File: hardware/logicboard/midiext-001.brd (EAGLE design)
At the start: 72 x 72 mm, 19 parts, among them IC1 74LS07N, IC2 LTC485N, IC3 LTC485N, X1 JST-2PINPH

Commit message: New schematic.
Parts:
- removed C6: 103, rcl:C025-025X050
- removed J5, J6: (no value), SparkFun-Connectors:2X4
- removed X1: JST-2PINPH, con-jst:B2B-PH
- added CN1, CN3, CN4: (no value), adafruit:JST-PH-2-SMT-RA
- added CN2, CN5: (no value), adafruit:JSTPH3
- moved IC2 33.9 mm to (41.9, 19.1)
- moved IC3 33.9 mm to (34.3, 52.1)
- renumbered D2 to D1, R10 to R2, R6 to R3, R7 to R1, R8 to R5, R9 to R4
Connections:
- removed net COM3: IC2.4
- removed net COM4: IC3.1
- removed net COM5: J6.8
- removed net VDD: X1.P1
- net COM1: now also IC2.1
- net COM2: now also IC3.4
- net GND: now also CN1.2, CN2.2, CN5.2, IC2.2, IC2.3, IC2.4; no longer C6.2, IC3.2, IC3.3, IC3.4, J5.2, J6.2, X1.P2
- net MIDIRX+: now also CN3.1; no longer J6.4
- net MIDIRX-: now also CN3.2; no longer J6.5
- net MIDITX+: now also CN2.1, R2.1; no longer J5.4, R2.2
- net MIDITX-: now also CN2.3; no longer J5.5
- net RX+: now also CN4.1, IC2.6; no longer IC3.6, J6.6
- net RX-: now also CN4.2, IC2.7; no longer IC3.7, J6.7
- net TX+: now also CN5.1, IC3.6; no longer IC2.6, J5.6
- net TX-: now also CN5.3, IC3.7; no longer IC2.7, J5.7
- net VCC: now also CN1.1, IC3.2, IC3.3, R2.2; no longer C6.1, IC2.2, IC2.3, R2.1

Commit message: Changed connectors.
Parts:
- removed CN1, CN3, CN4: (no value), adafruit:JST-PH-2-SMT-RA
- removed CN2, CN5: (no value), adafruit:JSTPH3
- added J1, J2, J3: (no value), SparkFun-Connectors:JST-2-PTH
- added J4, J5: (no value), SparkFun-Connectors:JST-3-PTH
- added J6: (no value), SparkFun-Connectors:JST-4-PTH
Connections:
- net GND: now also J1.2, J4.2, J5.2; no longer CN1.2, CN2.2, CN5.2
- net MIDIRX+: now also J2.1; no longer CN3.1
- net MIDIRX-: now also J2.2; no longer CN3.2
- net MIDITX+: now also J4.1; no longer CN2.1
- net MIDITX-: now also J4.3; no longer CN2.3
- net RX+: now also J3.1; no longer CN4.1
- net RX-: now also J3.2; no longer CN4.2
- net TX+: now also J5.1; no longer CN5.1
- net TX-: now also J5.3; no longer CN5.3
- net VCC: now also J1.1; no longer CN1.1

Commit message: Now has LED indicator port.
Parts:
- added R6, R7, R9: 220, resistor:0204/5
- added R8: 120, resistor:0204/5
- IC1: value 74LS07N -> 74ALS05N; device 74xx-us:DIL14 -> 74xx-eu:DIL14
- J2: device SparkFun-Connectors:JST-2-PTH -> SparkFun-Connectors:JST-3-PTH
- J4: device SparkFun-Connectors:JST-3-PTH -> SparkFun-Connectors:JST-2-PTH
- J5: device SparkFun-Connectors:JST-3-PTH -> SparkFun-Connectors:JST-4-PTH
- J6: device SparkFun-Connectors:JST-4-PTH -> SparkFun-Connectors:JST-3-PTH
- R4: value 120 -> 220
- moved IC1 175.6 mm to (15.2, -119.4)
- moved R4 154.6 mm to (10.2, -137.2)
- moved R5 48.9 mm to (48.3, 12.7)
- moved J2 35.6 mm to (10.2, -63.5)
- moved J5 18.0 mm to (12.7, -99.1)
- moved J6 18.0 mm to (10.2, -81.3)
- moved J4 17.8 mm to (10.2, -45.7)
- moved J3 17.8 mm to (10.2, -27.9)
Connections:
- removed net COM1: IC1.1, IC2.1
- new net N$1: IC1.3, IC1.9, IC2.1
- new net N$10: J5.2, R9.2
- new net N$3: IC1.1, IC1.4, R4.1
- new net N$6: IC1.6, R7.1
- new net N$7: IC1.8, R6.1
- new net N$8: J5.4, R7.2
- new net N$9: J5.3, R6.2
- net COM2: now also IC1.5
- net GND: now also J2.2, J6.2, R9.1; no longer IC1.3, IC1.5, IC1.9, J4.2, J5.2
- net MIDIRX+: now also J3.1; no longer J2.1
- net MIDIRX-: now also J3.2; no longer J2.2
- net MIDITX+: now also J2.1; no longer J4.1
- net MIDITX-: now also J2.3; no longer J4.3
- net RX+: now also J4.1, R5.2; no longer J3.1, R4.2
- net RX-: now also J4.2, R5.1; no longer J3.2, R4.1
- net TX+: now also J6.1, R8.2; no longer J5.1, R5.2
- net TX-: now also J6.3, R8.1; no longer J5.3, R5.1
- net VCC: now also J5.1, R4.2

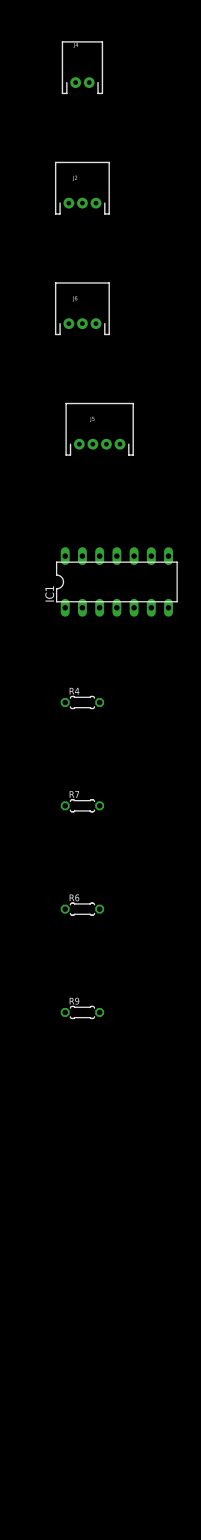
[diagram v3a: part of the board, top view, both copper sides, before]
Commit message: Now has LED indicator panel.
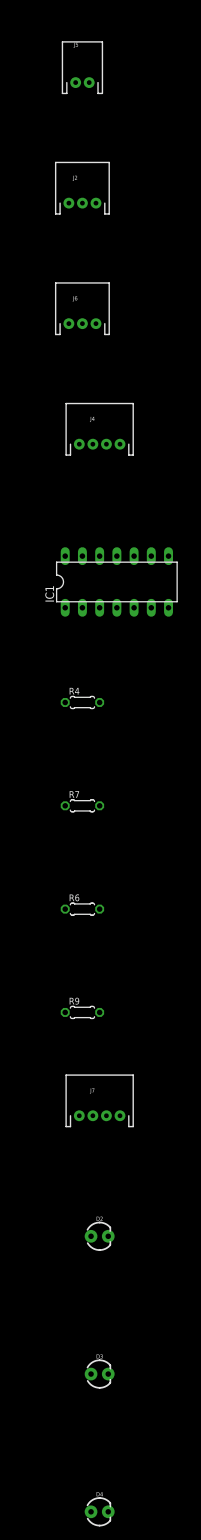
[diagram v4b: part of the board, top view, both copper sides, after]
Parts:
- added D2, D3, D4: (no value), SparkFun-LED:LED_3MM
- added J7: LED, SparkFun-Connectors:JST-4-PTH
- J1: value (none) -> PWR
- J2: value (none) -> MIDIOUT
- J3: value (none) -> MIDIIN
- J4: value (none) -> LED; device SparkFun-Connectors:JST-2-PTH -> SparkFun-Connectors:JST-4-PTH
- J5: value (none) -> MIDIRX; device SparkFun-Connectors:JST-4-PTH -> SparkFun-Connectors:JST-2-PTH
- J6: value (none) -> MIDITX
- moved J4 53.4 mm to (12.7, -99.1)
- moved J5 53.4 mm to (10.2, -45.7)
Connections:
- new net N$11: D3.K, J7.3
- new net N$12: D4.K, J7.4
- new net N$4: D2.A, D3.A, D4.A, J7.1
- new net N$5: D2.K, J7.2
- net N$10: now also J4.2; no longer J5.2
- net N$8: now also J4.4; no longer J5.4
- net N$9: now also J4.3; no longer J5.3
- net RX+: now also J5.1; no longer J4.1
- net RX-: now also J5.2; no longer J4.2
- net VCC: now also J4.1; no longer J5.1
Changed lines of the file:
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@@
 <element name="R1" library="resistor" library_urn="urn:adsk.eagle:library:348" package="0204/5" package3d_urn="urn:adsk.eagle:package:25955/1" value="220" x="40.64" y="63.5"/>
 <element name="R8" library="resistor" library_urn="urn:adsk.eagle:library:348" package="0204/5" package3d_urn="urn:adsk.eagle:package:25955/1" value="120" x="40.64" y="60.96"/>
-<element name="J1" library="SparkFun-Connectors" package="JST-2-PTH" value="" x="10.16" y="-10.16">
+<element name="J1" library="SparkFun-Connectors" package="JST-2-PTH" value="PWR" x="10.16" y="-10.16">
 <attribute name="PROD_ID" value="CONN-09863" x="10.16" y="-10.16" size="1.778" layer="27" display="off"/>
 <attribute name="SKU" value="PRT-09914" x="10.16" y="-10.16" size="1.778" layer="27" display="off"/>
 </element>
-<element name="J3" library="SparkFun-Connectors" package="JST-2-PTH" value="" x="10.16" y="-27.94">
+<element name="J3" library="SparkFun-Connectors" package="JST-2-PTH" value="MIDIIN" x="10.16" y="-27.94">
 <attribute name="PROD_ID" value="CONN-09863" x="10.16" y="-27.94" size="1.778" layer="27" display="off"/>
 <attribute name="SKU" value="PRT-09914" x="10.16" y="-27.94" size="1.778" layer="27" display="off"/>
 </element>
-<element name="J4" library="SparkFun-Connectors" package="JST-2-PTH" value="" x="10.16" y="-45.72">
+<element name="J5" library="SparkFun-Connectors" package="JST-2-PTH" value="MIDIRX" x="10.16" y="-45.72">
 <attribute name="PROD_ID" value="CONN-09863" x="10.16" y="-45.72" size="1.778" layer="27" display="off"/>
 <attribute name="SKU" value="PRT-09914" x="10.16" y="-45.72" size="1.778" layer="27" display="off"/>
 </element>
-<element name="J2" library="SparkFun-Connectors" package="JST-3-PTH" value="" x="10.16" y="-63.5">
+<element name="J2" library="SparkFun-Connectors" package="JST-3-PTH" value="MIDIOUT" x="10.16" y="-63.5">
 <attribute name="PROD_ID" value="WIRE-10037" x="10.16" y="-63.5" size="1.778" layer="27" display="off"/>
 <attribute name="SF_ID" value="PRT-09915" x="10.16" y="-63.5" size="1.778" layer="27" display="off"/>
 </element>
-<element name="J6" library="SparkFun-Connectors" package="JST-3-PTH" value="" x="10.16" y="-81.28">
+<element name="J6" library="SparkFun-Connectors" package="JST-3-PTH" value="MIDITX" x="10.16" y="-81.28">
 <attribute name="PROD_ID" value="WIRE-10037" x="10.16" y="-81.28" size="1.778" layer="27" display="off"/>
 <attribute name="SF_ID" value="PRT-09915" x="10.16" y="-81.28" size="1.778" layer="27" display="off"/>
 </element>
-<element name="J5" library="SparkFun-Connectors" package="JST-4-PTH" value="" x="12.7" y="-99.06">
+<element name="J4" library="SparkFun-Connectors" package="JST-4-PTH" value="LED" x="12.7" y="-99.06">
 <attribute name="PROD_ID" value="WIRE-13531" x="12.7" y="-99.06" size="1.778" layer="27" display="off"/>
 <attribute name="SF_ID" value="PRT-09916" x="12.7" y="-99.06" size="1.778" layer="27" display="off"/>
@@
 <element name="R6" library="resistor" library_urn="urn:adsk.eagle:library:348" package="0204/5" package3d_urn="urn:adsk.eagle:package:25955/1" value="220" x="10.16" y="-167.64"/>
 <element name="R9" library="resistor" library_urn="urn:adsk.eagle:library:348" package="0204/5" package3d_urn="urn:adsk.eagle:package:25955/1" value="220" x="10.16" y="-182.88"/>
+<element name="J7" library="SparkFun-Connectors" package="JST-4-PTH" value="LED" x="12.7" y="-198.12">
+<attribute name="PROD_ID" value="WIRE-13531" x="12.7" y="-198.12" size="1.778" layer="27" display="off"/>
+<attribute name="SF_ID" value="PRT-09916" x="12.7" y="-198.12" size="1.778" layer="27" display="off"/>
+</element>
+<element name="D2" library="SparkFun-LED" package="LED_3MM" value="" x="12.7" y="-215.9">
+<attribute name="PROD_ID" value="DIO-08794" x="12.7" y="-215.9" size="1.778" layer="27" display="off"/>
+</element>
+<element name="D3" library="SparkFun-LED" package="LED_3MM" value="" x="12.7" y="-236.22">
+<attribute name="PROD_ID" value="DIO-08794" x="12.7" y="-236.22" size="1.778" layer="27" display="off"/>
+</element>
+<element name="D4" library="SparkFun-LED" package="LED_3MM" value="" x="12.7" y="-256.54">
+<attribute name="PROD_ID" value="DIO-08794" x="12.7" y="-256.54" size="1.778" layer="27" display="off"/>
+</element>
 </elements>
 <signals>
@@
 <contactref element="IC1" pad="14"/>
 <contactref element="R4" pad="2"/>
-<contactref element="J5" pad="1"/>
+<contactref element="J4" pad="1"/>
 <wire x1="7.62" y1="-115.57" x2="12.7" y2="-137.16" width="0" layer="19" extent="1-1"/>
 <wire x1="9.7" y1="-99.06" x2="7.62" y2="-115.57" width="0" layer="19" extent="1-1"/>
@@
 <contactref element="R5" pad="2"/>
 <contactref element="IC2" pad="6"/>
-<contactref element="J4" pad="1"/>
+<contactref element="J5" pad="1"/>
 <wire x1="50.8" y1="12.7" x2="43.18" y2="22.86" width="0" layer="19" extent="1-1"/>
 <wire x1="9.16" y1="-45.72" x2="50.8" y2="12.7" width="0" layer="19" extent="1-1"/>
@@
 <contactref element="R5" pad="1"/>
 <contactref element="IC2" pad="7"/>
-<contactref element="J4" pad="2"/>
+<contactref element="J5" pad="2"/>
 <wire x1="45.72" y1="12.7" x2="40.64" y2="22.86" width="0" layer="19" extent="1-1"/>
 <wire x1="11.16" y1="-45.72" x2="45.72" y2="12.7" width="0" layer="19" extent="1-1"/>
@@
 </signal>
 <signal name="N$8">
-<contactref element="J5" pad="4"/>
+<contactref element="J4" pad="4"/>
 <contactref element="R7" pad="2"/>
 <wire x1="15.7" y1="-99.06" x2="12.7" y2="-152.4" width="0" layer="19" extent="1-1"/>
 </signal>
 <signal name="N$9">
-<contactref element="J5" pad="3"/>
+<contactref element="J4" pad="3"/>
 <contactref element="R6" pad="2"/>
 <wire x1="13.7" y1="-99.06" x2="12.7" y2="-167.64" width="0" layer="19" extent="1-1"/>
 </signal>
 <signal name="N$10">
-<contactref element="J5" pad="2"/>
+<contactref element="J4" pad="2"/>
 <contactref element="R9" pad="2"/>
 <wire x1="11.7" y1="-99.06" x2="12.7" y2="-182.88" width="0" layer="19" extent="1-1"/>
 </signal>
+<signal name="N$4">
+<contactref element="J7" pad="1"/>
+<contactref element="D4" pad="A"/>
+<contactref element="D3" pad="A"/>
+<contactref element="D2" pad="A"/>
+<wire x1="11.43" y1="-236.22" x2="11.43" y2="-256.54" width="0" layer="19" extent="1-1"/>
+<wire x1="11.43" y1="-215.9" x2="11.43" y2="-236.22" width="0" layer="19" extent="1-1"/>
+<wire x1="9.7" y1="-198.12" x2="11.43" y2="-215.9" width="0" layer="19" extent="1-1"/>
+</signal>
+<signal name="N$5">
+<contactref element="J7" pad="2"/>
+<contactref element="D2" pad="K"/>
+<wire x1="11.7" y1="-198.12" x2="13.97" y2="-215.9" width="0" layer="19" extent="1-1"/>
+</signal>
+<signal name="N$11">
+<contactref element="J7" pad="3"/>
+<contactref element="D3" pad="K"/>
+<wire x1="13.7" y1="-198.12" x2="13.97" y2="-236.22" width="0" layer="19" extent="1-1"/>
+</signal>
+<signal name="N$12">
+<contactref element="J7" pad="4"/>
+<contactref element="D4" pad="K"/>
+<wire x1="15.7" y1="-198.12" x2="13.97" y2="-256.54" width="0" layer="19" extent="1-1"/>
+</signal>
 </signals>

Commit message: First try.
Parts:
- D2: value (none) -> PWR
- D3: value (none) -> OUT
- D4: value (none) -> IN
- J7: device SparkFun-Connectors:JST-4-PTH -> SparkFun-Connectors:JST-4-PTH-VERT
- moved D4 287.1 mm to (5.08, 30.5)
- moved D3 271.9 mm to (5.08, 35.6)
- moved D2 256.7 mm to (5.08, 40.6)
- moved J7 233.7 mm to (10.2, 35.6), turned to 270 degrees
- moved R9 226.7 mm to (48.3, 40.6), turned to 180 degrees
- moved R6 214.2 mm to (48.3, 43.2), turned to 180 degrees
- moved R7 201.8 mm to (48.3, 45.7), turned to 180 degrees
- moved R4 179.4 mm to (48.3, 38.1)
- moved IC1 155.3 mm to (55.9, 30.5)
- moved J4 137.5 mm to (40.6, 35.6), turned to 90 degrees
- moved J6 106.1 mm to (40.6, 20.3), turned to 90 degrees
- moved J3 102.9 mm to (66.0, 58.4), turned to 270 degrees
- moved J2 96.6 mm to (66.0, 15.2), turned to 270 degrees
- moved J1 75.0 mm to (40.6, 58.4), turned to 90 degrees
- moved J5 65.9 mm to (40.6, 12.7), turned to 90 degrees
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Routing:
- net GND: track 0.00 -> 129.3 mm
- net VCC: track 0.00 -> 107.5 mm
- net TX+: track 0.00 -> 54.0 mm
- net TX-: track 0.00 -> 47.2 mm
- net N$1: track 0.00 -> 36.7 mm
- net COM2: track 0.00 -> 33.2 mm
- net N$6: track 0.00 -> 23.4 mm
- net N$15: track 0.00 -> 23.1 mm
- net N$3: track 0.00 -> 21.6 mm
- net RX+: track 0.00 -> 21.5 mm
- net MIDIRX-: track 0.00 -> 20.2 mm
- net RX-: track 0.00 -> 18.5 mm
- net N$7: track 0.00 -> 16.6 mm
- net N$4: track 0.00 -> 15.7 mm
- net N$2: track 0.00 -> 14.6 mm
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
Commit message: Second try.
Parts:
- moved C1 11.5 mm to (45.7, 59.7), turned to 270 degrees
- moved R1 4.58 mm to (61.0, 16.5)
- moved R3 3.81 mm to (58.4, 54.6)
- moved R2 3.81 mm to (58.4, 16.5)
- moved C2 3.59 mm to (55.9, 41.9)
- moved OK1 3.59 mm to (62.2, 41.9)
- moved IC1 2.84 mm to (58.4, 29.2)
- moved C4 2.54 mm to (45.7, 16.5)
- moved IC2 2.54 mm to (52.1, 16.5)
- moved C3 2.54 mm to (45.7, 54.6)
- moved C5 2.54 mm to (48.3, 29.2)
- moved D1 2.54 mm to (61.0, 54.6)
- moved IC3 2.54 mm to (52.1, 54.6)
- moved R5 2.54 mm to (45.7, 22.9), turned to 90 degrees
- moved R8 2.54 mm to (53.3, 61.0)
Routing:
- net COM2: track 33.2 -> 52.0 mm
- net VCC: track 107.5 -> 101.5 mm
- net TX+: track 54.0 -> 48.9 mm
- net N$2: track 14.6 -> 10.4 mm
- net TX-: track 47.2 -> 43.0 mm
- net RX+: track 21.5 -> 25.5 mm
- net MIDITX-: track 8.91 -> 5.37 mm
- net N$7: track 16.6 -> 19.6 mm
- net RX-: track 18.5 -> 15.5 mm
- net N$1: track 36.7 -> 34.1 mm
- net MIDIRX-: track 20.2 -> 22.6 mm
- net N$6: track 23.4 -> 25.7 mm
- net N$3: track 21.6 -> 23.2 mm
- net MIDIRX+: track 9.10 -> 10.7 mm
- net MIDITX+: track 7.86 -> 9.00 mm
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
